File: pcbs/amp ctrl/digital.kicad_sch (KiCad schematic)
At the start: 97 parts, among them J14 RF_Shield_Two_Pieces, U11 LT1880, U12 74LVC1G04, U6 LTC6220/LT6202, U8 AD5676, U90 ADS8168/ADS8167

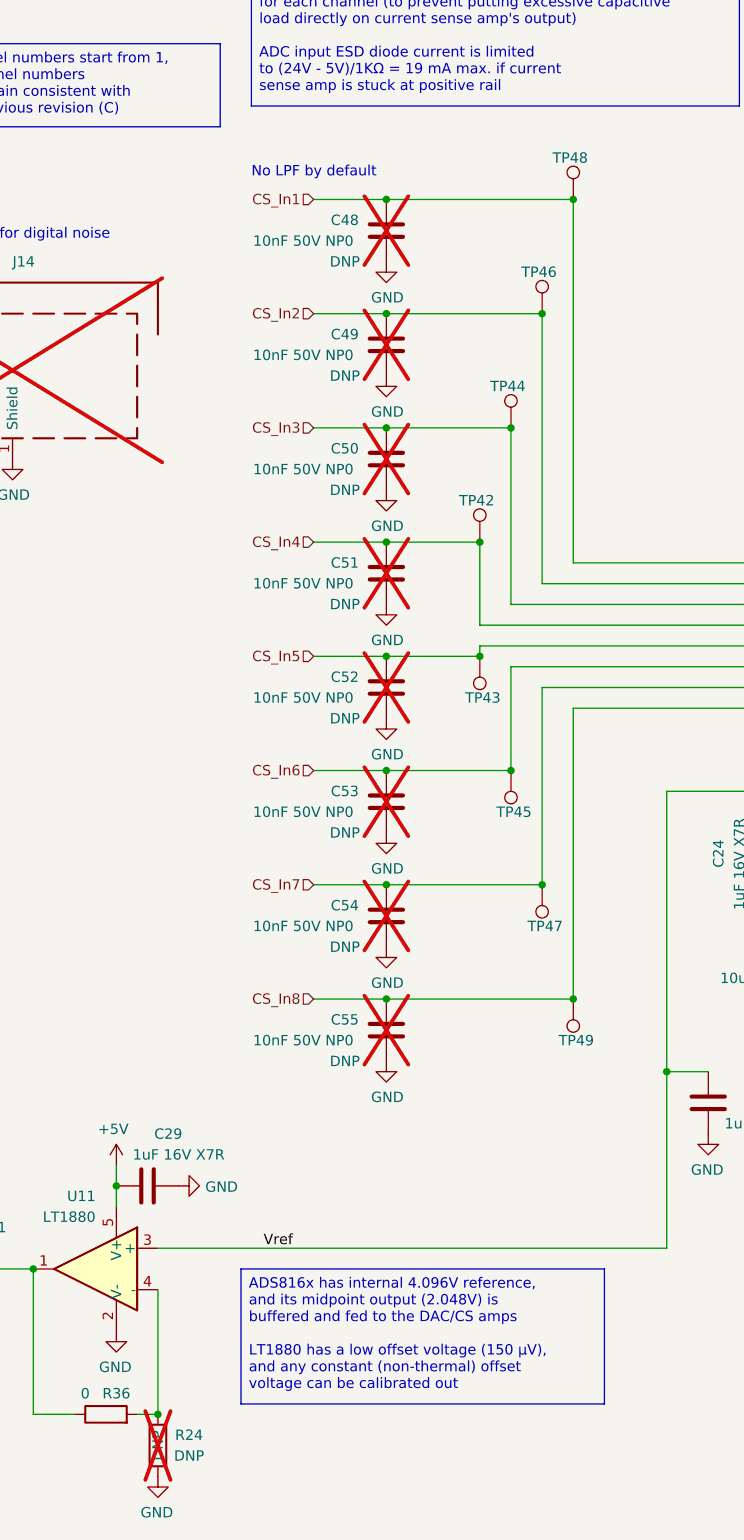
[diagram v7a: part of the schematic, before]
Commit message: BOM & reset fixes
Amp ctrl: changed name of "Manufacturer" field to "MPN" to work with Aisler
Amp ctrl: added part number to logic inverter, corrected various typos and part number problems
Backplane: added pull-down to Shutdown_Reset signal (#35)
Backplane: rethought Shutdown_Force circuit to make fail-safe (broken connections->shutdown), make work correctly (fixes #35)
Backplane: updated/corrected various schematic annotations
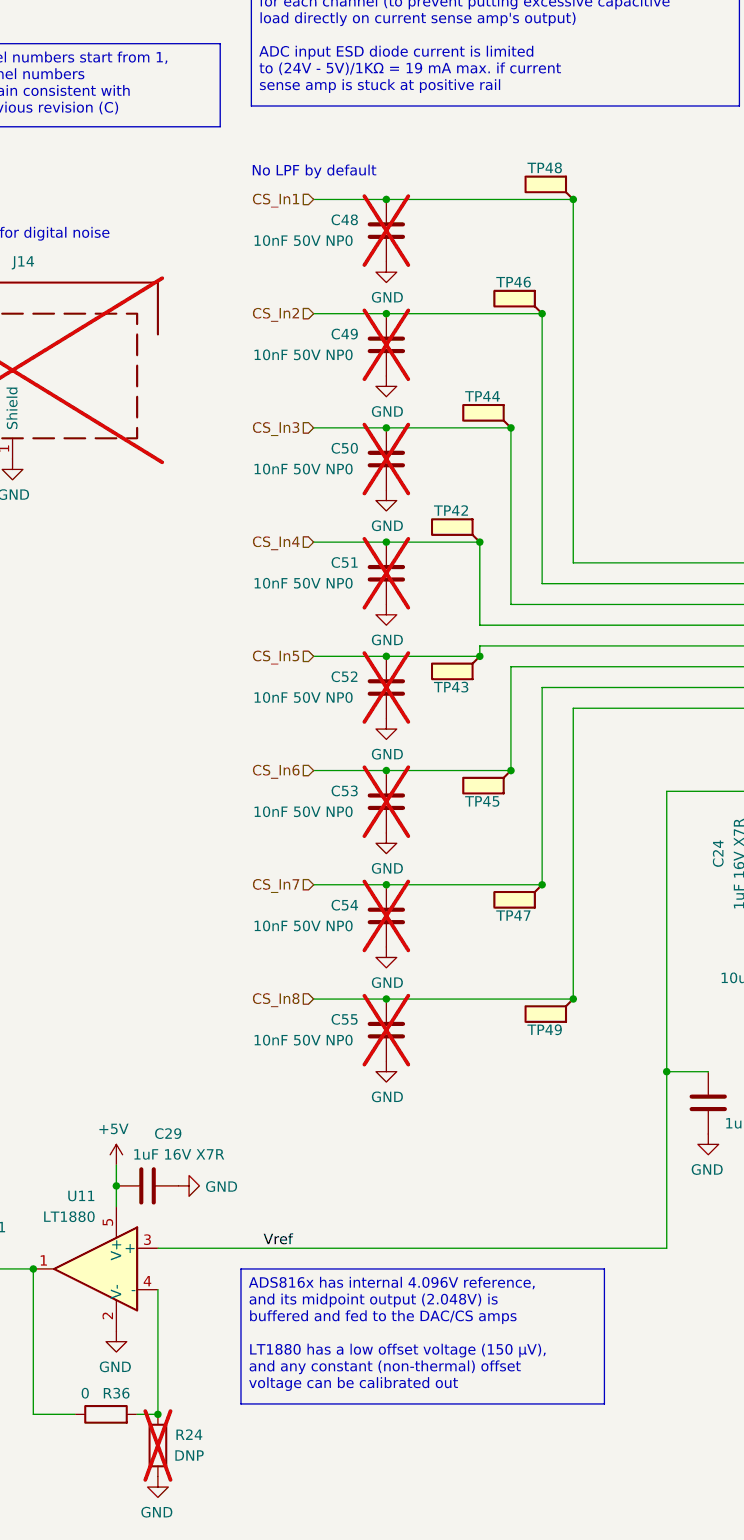
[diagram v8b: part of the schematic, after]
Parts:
- removed TP42, TP43, TP44, TP45, TP46, TP47, TP48, TP49: TestPoint_Flag, TestPoint:TestPoint_Pad_1.0x1.0mm, symbol Connector:TestPoint
- added TP42, TP43, TP44, TP45, TP46, TP47, TP48, TP49: TestPoint_Flag, TestPoint:TestPoint_Keystone_5019_Miniature, symbol Connector:TestPoint_Flag
- C20, C202, C22, C24, C25, C27, C29, C57, C59: MPN (none) -> C0603C105K4RACTU; Part Number C0603C105K4RACTU -> (none)
- C203: MPN (none) -> C0805C106M4PACTU; Part Number C0805C106M4PACTU -> (none)
- C26, C31: MPN (none) -> GRM1885C1H122JA01J; Part Number GRM1885C1H122JA01J -> (none)
- C28, C282: MPN (none) -> C0603C104K5RACTU; Part Number C0603C104K5RACTU -> (none)
- C32, C33, C34, C35, C36, C37, C38, C39, C40, C41, C42, C43, C44, C45, C46, C47: MPN (none) -> GRM1885C1H103JA01D; Part Number GRM1885C1H103JA01D -> (none)
- C48, C49, C50, C51, C52, C53, C54, C55: DNP DNP -> (none); MPN (none) -> GRM1885C1H103JA01D; Part Number GRM1885C1H103JA01D -> (none)
- J14: MPN (none) -> 36107406S, 36007400S; Part Number 36107406S, 36007400S -> (none)
- R21, R55: MPN (none) -> RK73H2ATTD10R0F; Part Number RK73H2ATTD10R0F -> (none)
- R22, R23: MPN (none) -> RK73H2ATTD30R0F; Part Number RK73H2ATTD30R0F -> (none)
- R24, R46, R47, R48, R49, R50, R51, R52: DNP DNP -> (none)
- R26, R27, R28, R29, R30, R31, R32, R33, R37, R38, R39, R40, R42, R43, R44, R45: MPN (none) -> RK73H2ATTD1001F; Part Number RK73H2ATTDD1001F -> (none)
- R288, R36: MPN (none) -> 5106; Part Number 5106 -> (none)
- TP22, TP23, TP24, TP25, TP26, TP27, TP28, TP29: MPN (none) -> 5019; Part Number 5019 -> (none)
- TP30, TP32, TP60, TP61: DNP DNP -> (none); MPN (none) -> 5019; Part Number 5019 -> (none)
- U11: MPN (none) -> LT1880IS5#TRMPBF; Part Number LT1880IS5#TRMPBF -> (none)
- U12: MPN (none) -> SN74LVC1G04DBVR; Manufacturer (none) -> Texas Instruments
- U6: MPN (none) -> LT6220CS5#TRMPBF; MPN Alt. (none) -> LT6220CS5#TRPBF, LT6220IS5#TRMPBF, LT6202HS5#TRMPBF, LT6202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; Part Number LT6220CS5#TRMPBF -> (none); Part Number Alt. LT6220CS5#TRPBF, LT6220IS5#TRMPBF, LT6202HS5#TRMPBF, LT6202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 -> (none)
- U8: MPN (none) -> AD5676ARUZ-REEL7; MPN Alt. (none) -> AD5676ARUZ, AD5676BRUZ-REEL7, AD5676BRUZ; Part Number AD5676ARUZ-REEL7 -> (none); Part Number Alt. AD5676ARUZ, AD5676BRUZ-REEL7, AD5676BRUZ -> (none)
- U90: MPN (none) -> ADS8168IRHBT; MPN Alt. (none) -> ADS8168IRHBR, ADS8167IRHBT, ADS8167IRHBR; Part Number ADS8168IRHBT -> (none); Part Number Alt. ADS8168IRHBR, ADS8167IRHBT, ADS8167IRHBR -> (none)
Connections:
- net CS_In1: now also TP48.1
- net CS_In2: now also TP46.1
- net CS_In3: now also TP44.1
- net CS_In4: now also TP42.1
- net CS_In5: now also TP43.1
- net CS_In6: now also TP45.1
- net CS_In7: now also TP47.1
- net CS_In8: now also TP49.1
